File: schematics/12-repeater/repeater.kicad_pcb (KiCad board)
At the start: 4 copper layers, 48.5 x 20.5 mm, 9 parts, among them J1 Cat5, J2 PSG01571, U1 PCA9600D

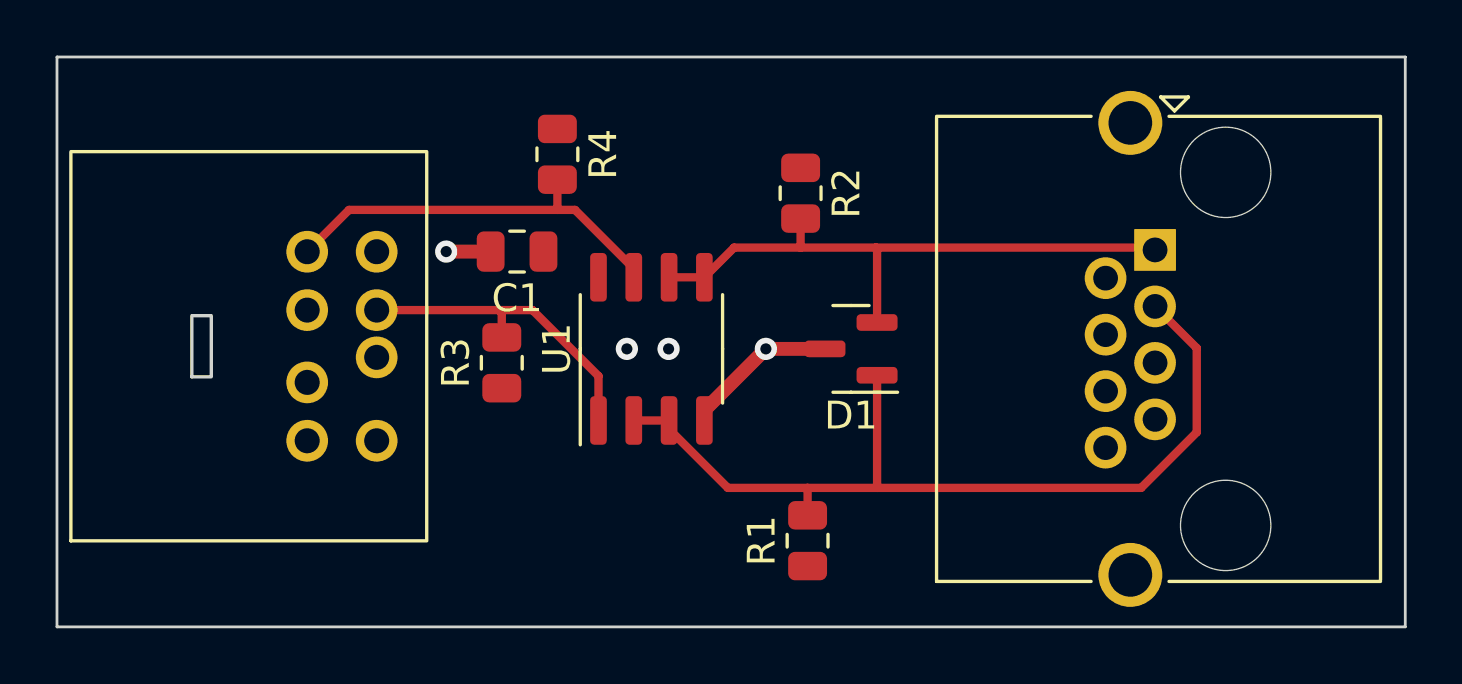
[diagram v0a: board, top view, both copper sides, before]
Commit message: added BZX84-C15 diodes, 1.8v not fixed
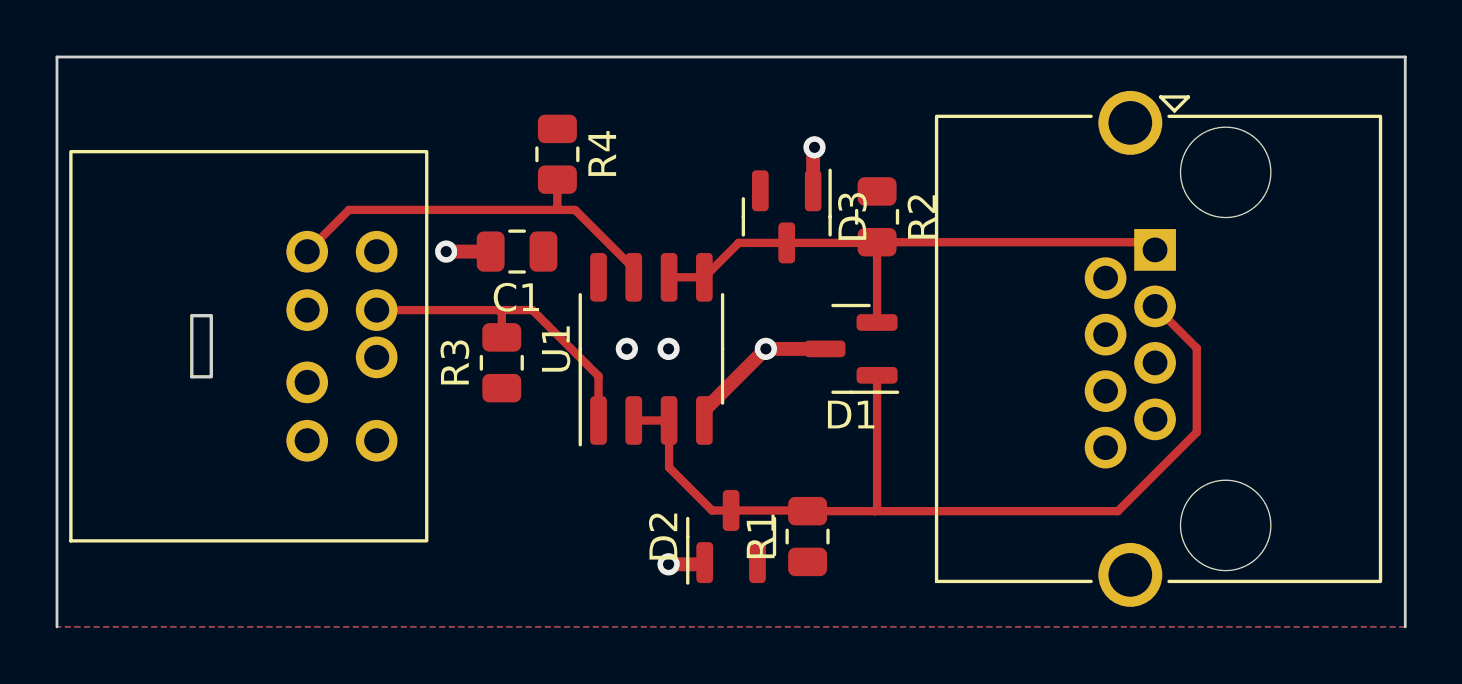
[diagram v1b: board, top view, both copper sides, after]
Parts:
- added D2: Diode_Zener_BZX84-C15, Package_TO_SOT_SMD:SOT-23, F.Cu at (146.2, 90.2)
- added D3: Diode_Zener_BZX84-C15, Package_TO_SOT_SMD:SOT-23, F.Cu at (148.2, 78.8)
- moved R2 2.88 mm to (151.5, 78.8)
- moved R1 0.15 mm to (149.0, 90.2)
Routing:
- net GND: track 7.22 -> 10.1 mm, vias 2 -> 4
- net /SDA_D: track 32.5 -> 33.8 mm
- net /SCL_D: track 21.7 -> 21.0 mm

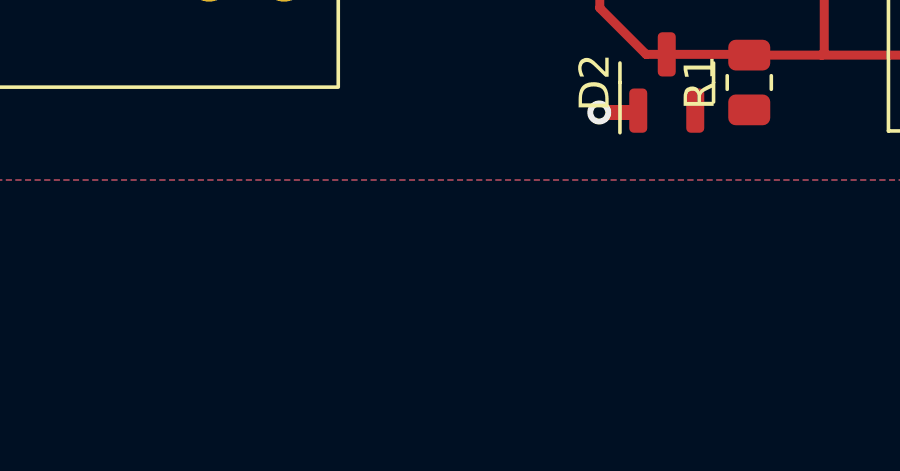
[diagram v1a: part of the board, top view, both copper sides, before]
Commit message: added mounting holes
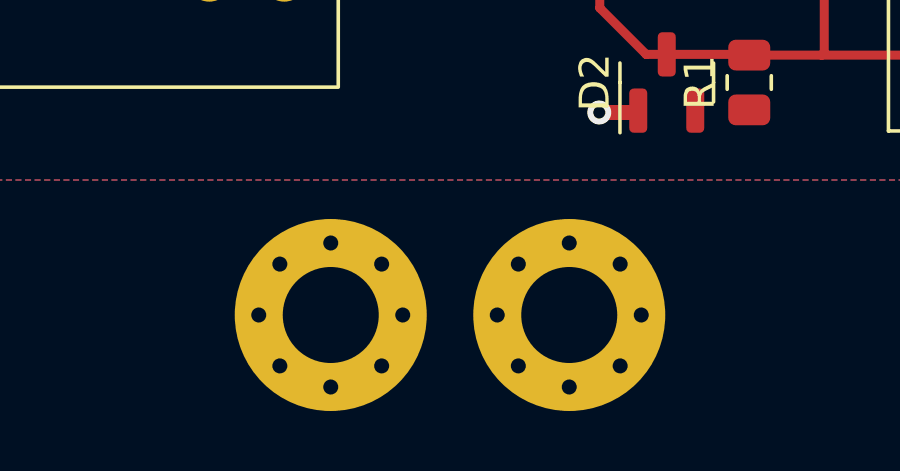
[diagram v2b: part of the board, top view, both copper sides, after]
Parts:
- added H1: MountingHole_Pad, royale:MountingHole_Pad, F.Cu at (143.0, 98.0)
- added H2: MountingHole_Pad, royale:MountingHole_Pad, F.Cu at (135.1, 98.0)
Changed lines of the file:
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@@
   (net 5 "/SDA")
   (net 6 "/SCL")
+  (footprint "royale:MountingHole_Pad" (layer "F.Cu")
+    (at 143 98)
+    (property "Sheetfile" "repeater.kicad_sch")
+    (property "Sheetname" "")
+    (attr exclude_from_pos_files)
+    (fp_text reference "H1" (at 0 -4.2) (layer "F.SilkS") hide
+      (effects (font (size 1 1) (thickness 0.15)))
+    )
+    (fp_text value "MountingHole_Pad" (at 0 4.2) (layer "F.Fab")
+      (effects (font (size 1 1) (thickness 0.15)))
+    )
+    (fp_text user "${REFERENCE}" (at 0.3 0) (layer "F.Fab")
+      (effects (font (size 1 1) (thickness 0.15)))
+    )
+    (fp_circle (center 0 0) (end 3.2 0) (layer "Cmts.User") (width 0.15) (fill none))
+    (fp_circle (center 0 0) (end 3.45 0) (layer "F.CrtYd") (width 0.05) (fill none))
+    (pad "1" thru_hole circle locked (at -1.697056 1.697056) (size 0.8 0.8) (drill 0.5) (layers *.Cu *.Mask)
+      (net 2 "GND") (pinfunction "1") (pintype "input"))
+    (pad "1" thru_hole circle locked (at -1.697056 -1.697056) (size 0.8 0.8) (drill 0.5) (layers *.Cu *.Mask)
+      (net 2 "GND") (pinfunction "1") (pintype "input"))
+    (pad "1" thru_hole circle locked (at 0 -2.4) (size 0.8 0.8) (drill 0.5) (layers *.Cu *.Mask)
+      (net 2 "GND") (pinfunction "1") (pintype "input"))
+    (pad "1" thru_hole circle locked (at 1.697056 -1.697056) (size 0.8 0.8) (drill 0.5) (layers *.Cu *.Mask)
+      (net 2 "GND") (pinfunction "1") (pintype "input"))
+    (pad "1" thru_hole circle locked (at -2.4 0) (size 0.8 0.8) (drill 0.5) (layers *.Cu *.Mask)
+      (net 2 "GND") (pinfunction "1") (pintype "input"))
+    (pad "1" thru_hole circle locked (at 0 0) (size 6.4 6.4) (drill 3.2) (layers *.Cu *.Mask)
+      (net 2 "GND") (pinfunction "1") (pintype "input"))
+    (pad "1" thru_hole circle locked (at 1.697056 1.697056) (size 0.8 0.8) (drill 0.5) (layers *.Cu *.Mask)
+      (net 2 "GND") (pinfunction "1") (pintype "input"))
+    (pad "1" thru_hole circle locked (at 2.4 0) (size 0.8 0.8) (drill 0.5) (layers *.Cu *.Mask)
+      (net 2 "GND") (pinfunction "1") (pintype "input"))
+    (pad "1" thru_hole circle locked (at 0 2.4) (size 0.8 0.8) (drill 0.5) (layers *.Cu *.Mask)
+      (net 2 "GND") (pinfunction "1") (pintype "input"))
+  )
   (footprint "Resistor_SMD:R_0805_2012Metric" (layer "F.Cu")
     (at 149 90.25 90)
@@
     )
   )
+  (footprint "royale:MountingHole_Pad" (layer "F.Cu")
+    (at 135.05 98)
+    (property "Sheetfile" "repeater.kicad_sch")
+    (property "Sheetname" "")
+    (attr exclude_from_pos_files)
+    (fp_text reference "H2" (at 0 -4.2) (layer "F.SilkS") hide
+      (effects (font (size 1 1) (thickness 0.15)))
+    )
+    (fp_text value "MountingHole_Pad" (at 0 4.2) (layer "F.Fab")
+      (effects (font (size 1 1) (thickness 0.15)))
+    )
+    (fp_text user "${REFERENCE}" (at 0.3 0) (layer "F.Fab")
+      (effects (font (size 1 1) (thickness 0.15)))
+    )
+    (fp_circle (center 0 0) (end 3.2 0) (layer "Cmts.User") (width 0.15) (fill none))
+    (fp_circle (center 0 0) (end 3.45 0) (layer "F.CrtYd") (width 0.05) (fill none))
+    (pad "1" thru_hole circle locked (at 0 -2.4) (size 0.8 0.8) (drill 0.5) (layers *.Cu *.Mask)
+      (net 2 "GND") (pinfunction "1") (pintype "input"))
+    (pad "1" thru_hole circle locked (at 1.697056 1.697056) (size 0.8 0.8) (drill 0.5) (layers *.Cu *.Mask)
+      (net 2 "GND") (pinfunction "1") (pintype "input"))
+    (pad "1" thru_hole circle locked (at -1.697056 -1.697056) (size 0.8 0.8) (drill 0.5) (layers *.Cu *.Mask)
+      (net 2 "GND") (pinfunction "1") (pintype "input"))
+    (pad "1" thru_hole circle locked (at 0 2.4) (size 0.8 0.8) (drill 0.5) (layers *.Cu *.Mask)
+      (net 2 "GND") (pinfunction "1") (pintype "input"))
+    (pad "1" thru_hole circle locked (at -1.697056 1.697056) (size 0.8 0.8) (drill 0.5) (layers *.Cu *.Mask)
+      (net 2 "GND") (pinfunction "1") (pintype "input"))
+    (pad "1" thru_hole circle locked (at -2.4 0) (size 0.8 0.8) (drill 0.5) (layers *.Cu *.Mask)
+      (net 2 "GND") (pinfunction "1") (pintype "input"))
+    (pad "1" thru_hole circle locked (at 2.4 0) (size 0.8 0.8) (drill 0.5) (layers *.Cu *.Mask)
+      (net 2 "GND") (pinfunction "1") (pintype "input"))
+    (pad "1" thru_hole circle locked (at 1.697056 -1.697056) (size 0.8 0.8) (drill 0.5) (layers *.Cu *.Mask)
+      (net 2 "GND") (pinfunction "1") (pintype "input"))
+    (pad "1" thru_hole circle locked (at 0 0) (size 6.4 6.4) (drill 3.2) (layers *.Cu *.Mask)
+      (net 2 "GND") (pinfunction "1") (pintype "input"))
+  )
   (footprint "Package_TO_SOT_SMD:SOT-23" (layer "F.Cu")

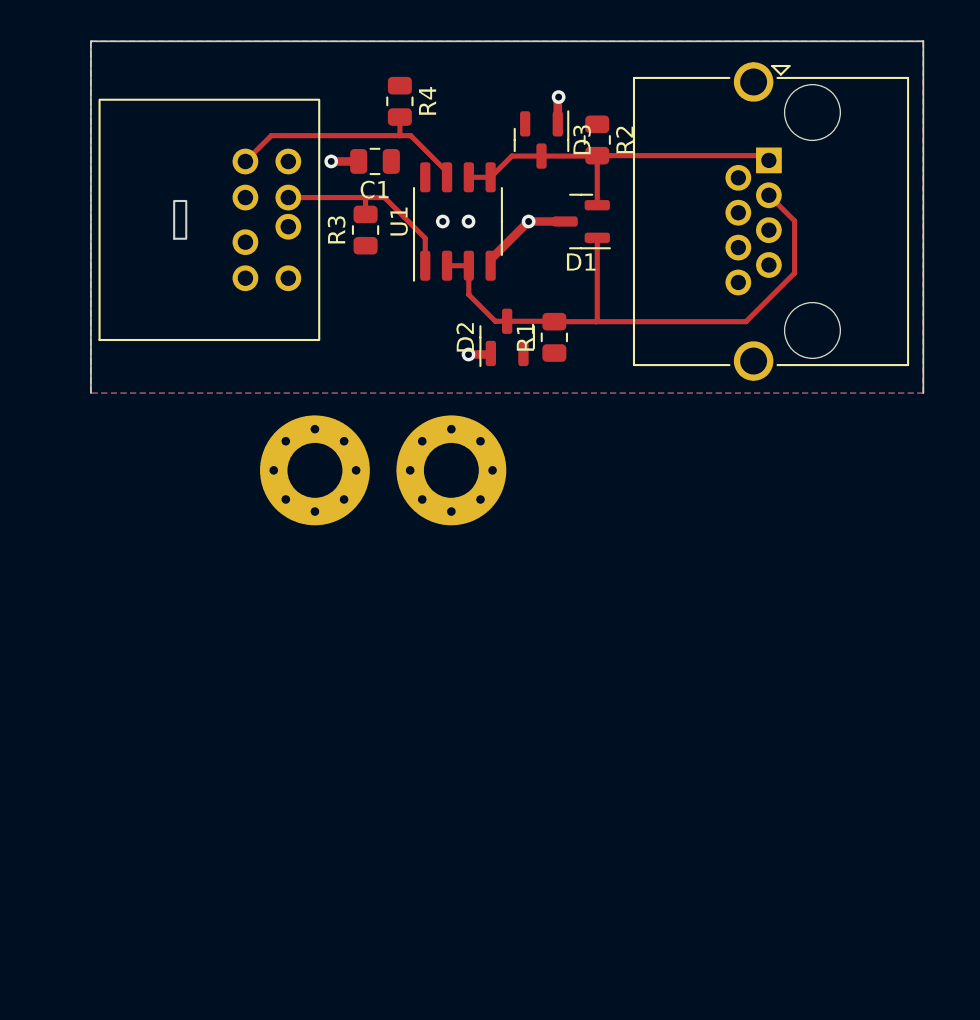
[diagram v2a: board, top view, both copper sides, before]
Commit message: added mounting holes
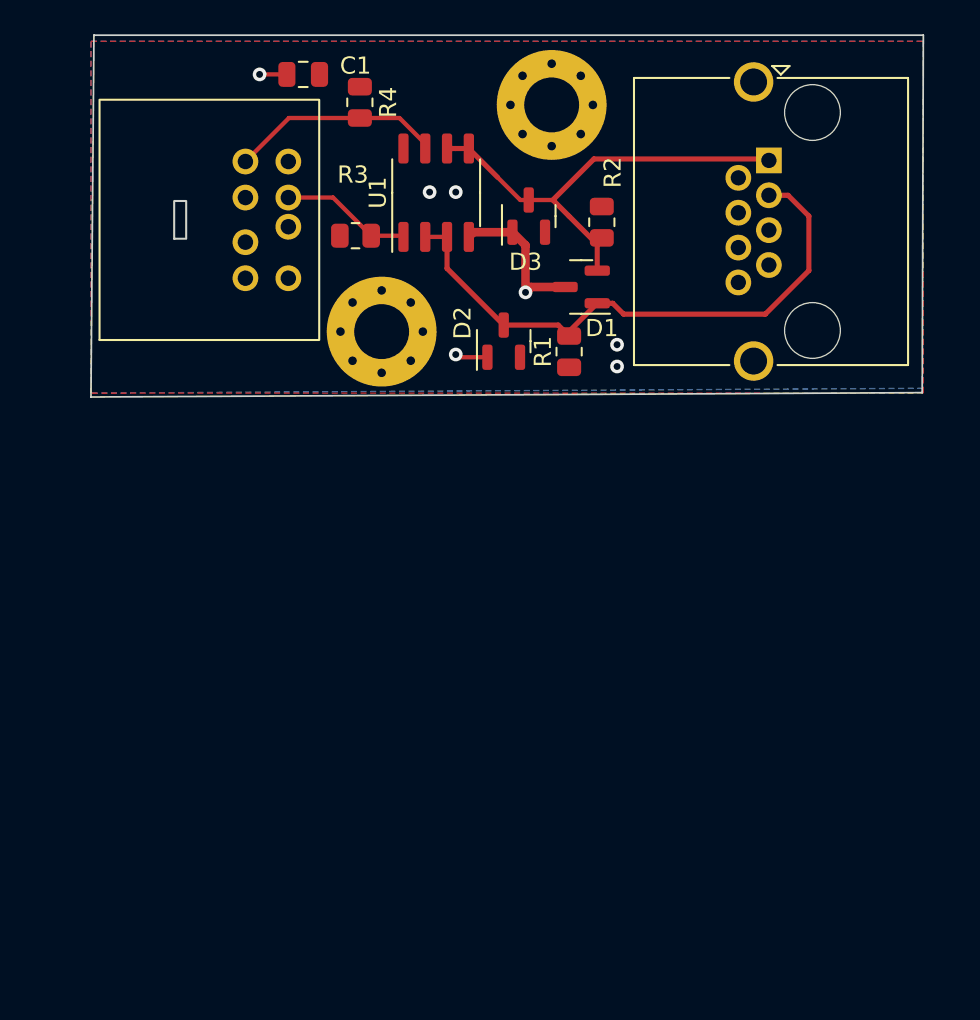
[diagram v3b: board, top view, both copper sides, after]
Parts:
- moved H1 22.1 mm to (148.8, 76.7)
- moved H2 8.97 mm to (138.9, 89.9)
- moved C1 6.57 mm to (134.4, 74.9)
- moved R2 4.80 mm to (151.8, 83.5)
- moved D3 4.50 mm to (147.5, 83.2), turned to 90 degrees
- moved D1 3.81 mm to (150.6, 87.3)
- moved R4 2.33 mm to (137.7, 76.6)
- moved U1 2.10 mm to (142.1, 81.8)
- moved R1 1.20 mm to (149.9, 91.1)
- moved R3 0.67 mm to (137.4, 84.3), turned to 0 degrees
- moved D2 0.30 mm to (146.1, 90.5)
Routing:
- net /SCL_D: track 21.0 -> 26.2 mm
- net /SDA: track 11.6 -> 7.66 mm
- net GND: track 10.1 -> 12.5 mm, vias 4 -> 3
- net /SCL: track 14.6 -> 12.4 mm
- net 1v8: vias 2 -> 4
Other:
- board size 48.5 x 20.5 mm -> 48.5 x 21.1 mm

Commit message: Refined repeater pcb
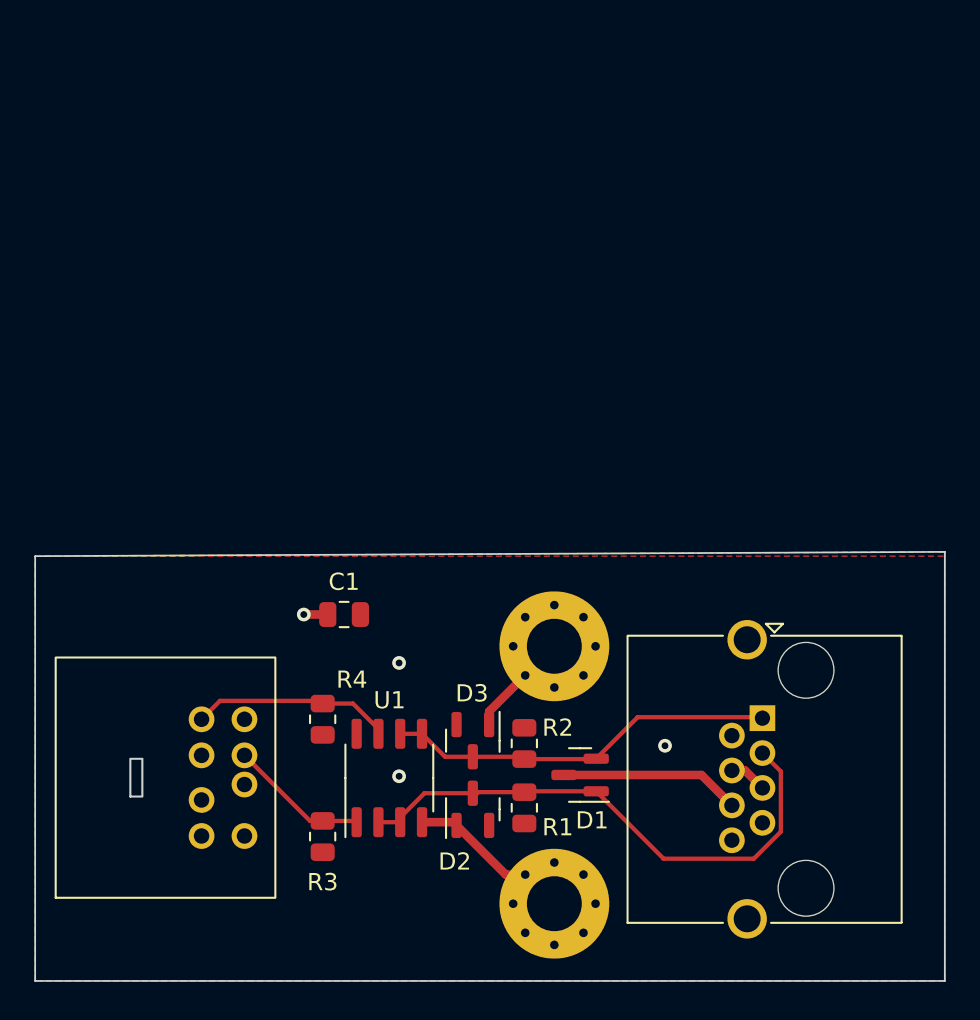
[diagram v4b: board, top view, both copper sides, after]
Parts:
- moved R4 36.0 mm to (135.5, 112.5), turned to 90 degrees
- moved R3 35.1 mm to (135.5, 119.3), turned to 90 degrees
- moved H2 34.8 mm to (149.0, 123.2)
- moved U1 34.2 mm to (139.4, 115.9)
- moved J2 32.6 mm to (119.9, 122.9)
- moved J1 32.5 mm to (161.1, 112.4)
- moved C1 31.6 mm to (136.8, 106.4)
- moved H1 31.5 mm to (149.0, 108.2)
- moved D3 30.7 mm to (144.2, 113.8), turned to -90 degrees
- moved R2 30.7 mm to (147.2, 113.9)
- moved D1 28.4 mm to (150.5, 115.8)
- moved D2 27.3 mm to (144.2, 117.8)
- moved R1 26.7 mm to (147.2, 117.7)
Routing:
- net GND: track 12.5 -> 25.3 mm, vias 3 -> 1
- net /SCL_D: track 26.2 -> 22.8 mm
- net /SDA_D: track 34.1 -> 31.8 mm
- net 1v8: track 0.00 -> 2.20 mm, vias 4 -> 3
- net /SCL: track 12.4 -> 11.7 mm
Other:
- board size 48.5 x 21.1 mm -> 53 x 25 mm

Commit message: Update repeater ready for manufacture
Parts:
- moved C1 9.44 mm to (134.7, 115.6), turned to -90 degrees
- moved H1 8.86 mm to (140.2, 107.5)
- moved R4 1.04 mm to (134.7, 111.9)
- moved R3 0.88 mm to (134.7, 119.1)
- moved D1 0.74 mm to (149.9, 115.2)
- moved D2 0.74 mm to (143.7, 117.2)
- moved D3 0.74 mm to (143.7, 113.2)
- moved J1 0.74 mm to (160.6, 111.9)
- moved R1 0.74 mm to (146.7, 117.2)
- moved R2 0.74 mm to (146.7, 113.4)
- moved U1 0.74 mm to (138.8, 115.4)
- moved H2 0.47 mm to (148.6, 123.5)
- moved J2 0.41 mm to (119.9, 122.5)
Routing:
- net GND: track 25.3 -> 17.5 mm, vias 1 -> 3
- net /SCL: track 11.7 -> 9.44 mm
- net 1v8: track 2.20 -> 0.00 mm, vias 3 -> 0
- net /SDA: track 8.15 -> 6.87 mm
- net /SDA_D: track 31.8 -> 32.4 mm
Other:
- board size 53 x 25 mm -> 50 x 25 mm
